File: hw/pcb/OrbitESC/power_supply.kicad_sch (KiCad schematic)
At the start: 0 parts

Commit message: Add power stage components
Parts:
- added C22, C24, C28: 100nF, Capacitor_SMD:C_0402_1005Metric, symbol Device:C
- added C23, C25, C26: 10uF, Capacitor_SMD:C_0805_2012Metric, symbol Device:C
- added C27, C29: 2.2uF, Capacitor_SMD:C_0805_2012Metric, symbol Device:C
- added D1, D3, D4: Blue LED, Diode_SMD:D_0603_1608Metric, symbol Device:LED
- added D2: 18v, Diode_SMD:D_SMA, symbol Device:D_Zener
- added FB1: FerriteBead_Small, Resistor_SMD:R_0603_1608Metric, symbol Device:FerriteBead_Small
- added L1: 4.7uH, Inductor_SMD:L_Bourns-SRN6028, symbol Device:L
- added Q7: 2N7002, Package_TO_SOT_SMD:SOT-23, symbol Transistor_FET:2N7002
- added R37, R38, R41, R44: 10k, Resistor_SMD:R_0402_1005Metric, symbol Device:R_US
- added R39: 1k, Resistor_SMD:R_0402_1005Metric, symbol Device:R_US
- added R40: 51k, Resistor_SMD:R_0402_1005Metric, symbol Device:R_US
- added R42: 10, Resistor_SMD:R_0402_1005Metric, symbol Device:R_US
- added R43: 1.5k, Resistor_SMD:R_0402_1005Metric, symbol Device:R_US
- added R45: 200, Resistor_SMD:R_0402_1005Metric, symbol Device:R_US
- added R46: 49.9, Resistor_SMD:R_0402_1005Metric, symbol Device:R_US
- added U7: AP62200Z6-7, Package_TO_SOT_SMD:SOT-563, symbol Regulator_Switching:AP62250Z6
- added U8: AP2171W, Package_TO_SOT_SMD:SOT-23-5, symbol Power_Management:AP2171W
- added U9: AP2120, Package_TO_SOT_SMD:SOT-23, symbol Regulator_Linear:AP2127N-3.3
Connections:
- new net: R37.2, U7.5 (EN)
- new net: D4.2 (A), R46.2
- new net: D3.2 (A), R45.2
- new net: R40.2, R41.2, U7.6 (FB)
- new net: C24.1, L1.1, U7.2 (SW)
- new net: C24.2, U7.4 (BST)
- new net: FB1.2, R42.1
- new net: D1.2 (A), R43.2
- new net: Q7.1 (G), R38.2, R39.2
- new net: Q7.3 (D), R44.2, U8.4 (EN)
- new net +3.3V: C29.2, FB1.1, R46.1, U9.2 (VO)
- new net +3.3VADC: C27.2, C28.1, R42.2
- new net +5V: C25.1, C26.1, L1.2, R40.1, R45.1, U8.1 (OUT), U9.3 (VI)
- new net GNDD: C22.1, C23.2, C25.2, C26.2, C27.1, C28.2, C29.1, D1.1 (K), D2.2 (A), D3.1 (K), D4.1 (K), Q7.2 (S), R38.1, R41.1, U7.3 (GND), U8.2 (GND), U9.1 (GND)
- new net VBUS: R44.1, U8.5 (IN)
- new net VDC: C22.2, C23.1, D2.1 (K), R37.1, R39.1, R43.1, U7.1 (VIN)
- no-connect marks 0 -> 1
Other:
- note added: "Buck Converter"
- note added: "USB Power Select"

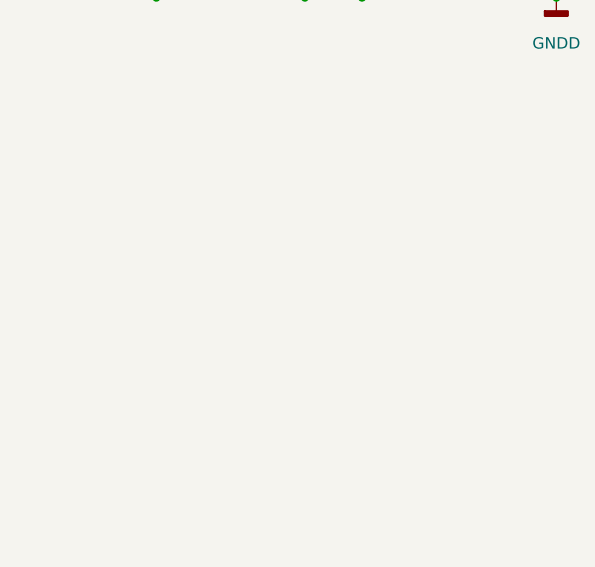
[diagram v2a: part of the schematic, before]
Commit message: Start routing power stage
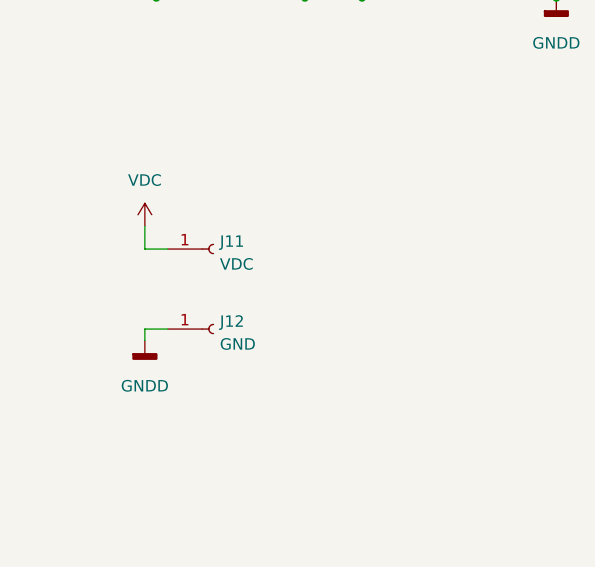
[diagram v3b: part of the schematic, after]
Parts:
- added J11: VDC, TestPoint:TestPoint_Pad_4.0x4.0mm, symbol Connector:Conn_01x01_Female
- added J12: GND, TestPoint:TestPoint_Pad_4.0x4.0mm, symbol Connector:Conn_01x01_Female
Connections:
- net GNDD: now also J12.1 (Pin_1)
- net VDC: now also J11.1 (Pin_1)
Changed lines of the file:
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@@
+    (stroke (width 0) (type default) (color 0 0 0 0))
+  )
+  (wire (pts (xy 54.61 95.25) (xy 54.61 97.79))
     (stroke (width 0) (type default) (color 0 0 0 0))
   )
@@
     (stroke (width 0) (type default) (color 0 0 0 0))
   )
+  (wire (pts (xy 54.61 106.68) (xy 57.15 106.68))
+    (stroke (width 0) (type default) (color 0 0 0 0))
+  )
   (wire (pts (xy 87.63 41.91) (xy 78.74 41.91))
     (stroke (width 0) (type default) (color 0 0 0 0))
@@
     (stroke (width 0) (type default) (color 0 0 0 0))
   )
+  (wire (pts (xy 54.61 107.95) (xy 54.61 106.68))
+    (stroke (width 0) (type default) (color 0 0 0 0))
+  )
   (wire (pts (xy 168.91 69.85) (xy 157.48 69.85))
     (stroke (width 0) (type default) (color 0 0 0 0))
@@
   )
   (wire (pts (xy 146.05 54.61) (xy 146.05 55.88))
+    (stroke (width 0) (type default) (color 0 0 0 0))
+  )
+  (wire (pts (xy 54.61 97.79) (xy 57.15 97.79))
     (stroke (width 0) (type default) (color 0 0 0 0))
   )
@@
     (pin "2")
   )
+  (symbol (lib_id "power:VDC") (at 54.61 95.25 0) (unit 1)
+    (in_bom yes) (on_board yes)
+    (property "Reference" "#PWR0139" (id 0) (at 54.61 97.79 0)
+      (effects (font (size 1.27 1.27)) hide)
+    )
+    (property "Value" "VDC" (id 1) (at 54.61 90.17 0))
+    (property "Footprint" "" (id 2) (at 54.61 95.25 0)
+      (effects (font (size 1.27 1.27)) hide)
+    )
+    (property "Datasheet" "" (id 3) (at 54.61 95.25 0)
+      (effects (font (size 1.27 1.27)) hide)
+    )
+    (pin "1")
+  )
   (symbol (lib_id "Regulator_Switching:AP62250Z6") (at 111.76 44.45 0) (unit 1)
     (in_bom yes) (on_board yes) (fields_autoplaced)
@@
     (pin "2")
   )
+  (symbol (lib_id "Connector:Conn_01x01_Female") (at 62.23 106.68 0) (unit 1)
+    (in_bom yes) (on_board yes) (fields_autoplaced)
+    (property "Reference" "J12" (id 0) (at 62.9412 105.8453 0)
+      (effects (font (size 1.27 1.27)) (justify left))
+    )
+    (property "Value" "GND" (id 1) (at 62.9412 108.3822 0)
+      (effects (font (size 1.27 1.27)) (justify left))
+    )
+    (property "Footprint" "TestPoint:TestPoint_Pad_4.0x4.0mm" (id 2) (at 62.23 106.68 0)
+      (effects (font (size 1.27 1.27)) hide)
+    )
+    (property "Datasheet" "~" (id 3) (at 62.23 106.68 0)
+      (effects (font (size 1.27 1.27)) hide)
+    )
+    (property "DigiKey" "N/A" (id 4) (at 62.23 106.68 0)
+      (effects (font (size 1.27 1.27)) hide)
+    )
+    (pin "1")
+  )
   (symbol (lib_id "Device:LED") (at 41.91 59.69 90) (unit 1)
     (in_bom yes) (on_board yes) (fields_autoplaced)
@@
     )
     (property "Datasheet" "" (id 3) (at 100.33 69.85 0)
+      (effects (font (size 1.27 1.27)) hide)
+    )
+    (pin "1")
+  )
+  (symbol (lib_id "Connector:Conn_01x01_Female") (at 62.23 97.79 0) (unit 1)
+    (in_bom yes) (on_board yes) (fields_autoplaced)
+    (property "Reference" "J11" (id 0) (at 62.9412 96.9553 0)
+      (effects (font (size 1.27 1.27)) (justify left))
+    )
+    (property "Value" "VDC" (id 1) (at 62.9412 99.4922 0)
+      (effects (font (size 1.27 1.27)) (justify left))
+    )
+    (property "Footprint" "TestPoint:TestPoint_Pad_4.0x4.0mm" (id 2) (at 62.23 97.79 0)
+      (effects (font (size 1.27 1.27)) hide)
+    )
+    (property "Datasheet" "~" (id 3) (at 62.23 97.79 0)
+      (effects (font (size 1.27 1.27)) hide)
+    )
+    (property "DigiKey" "N/A" (id 4) (at 62.23 97.79 0)
       (effects (font (size 1.27 1.27)) hide)
     )
@@
       (effects (font (size 1.27 1.27)) hide)
     )
+    (pin "1")
+  )
+  (symbol (lib_id "power:GNDD") (at 54.61 107.95 0) (unit 1)
+    (in_bom yes) (on_board yes) (fields_autoplaced)
+    (property "Reference" "#PWR0140" (id 0) (at 54.61 114.3 0)
+      (effects (font (size 1.27 1.27)) hide)
+    )
+    (property "Value" "GNDD" (id 1) (at 54.61 113.03 0))
+    (property "Footprint" "" (id 2) (at 54.61 107.95 0)
+      (effects (font (size 1.27 1.27)) hide)
+    )
+    (property "Datasheet" "" (id 3) (at 54.61 107.95 0)
+      (effects (font (size 1.27 1.27)) hide)
+    )

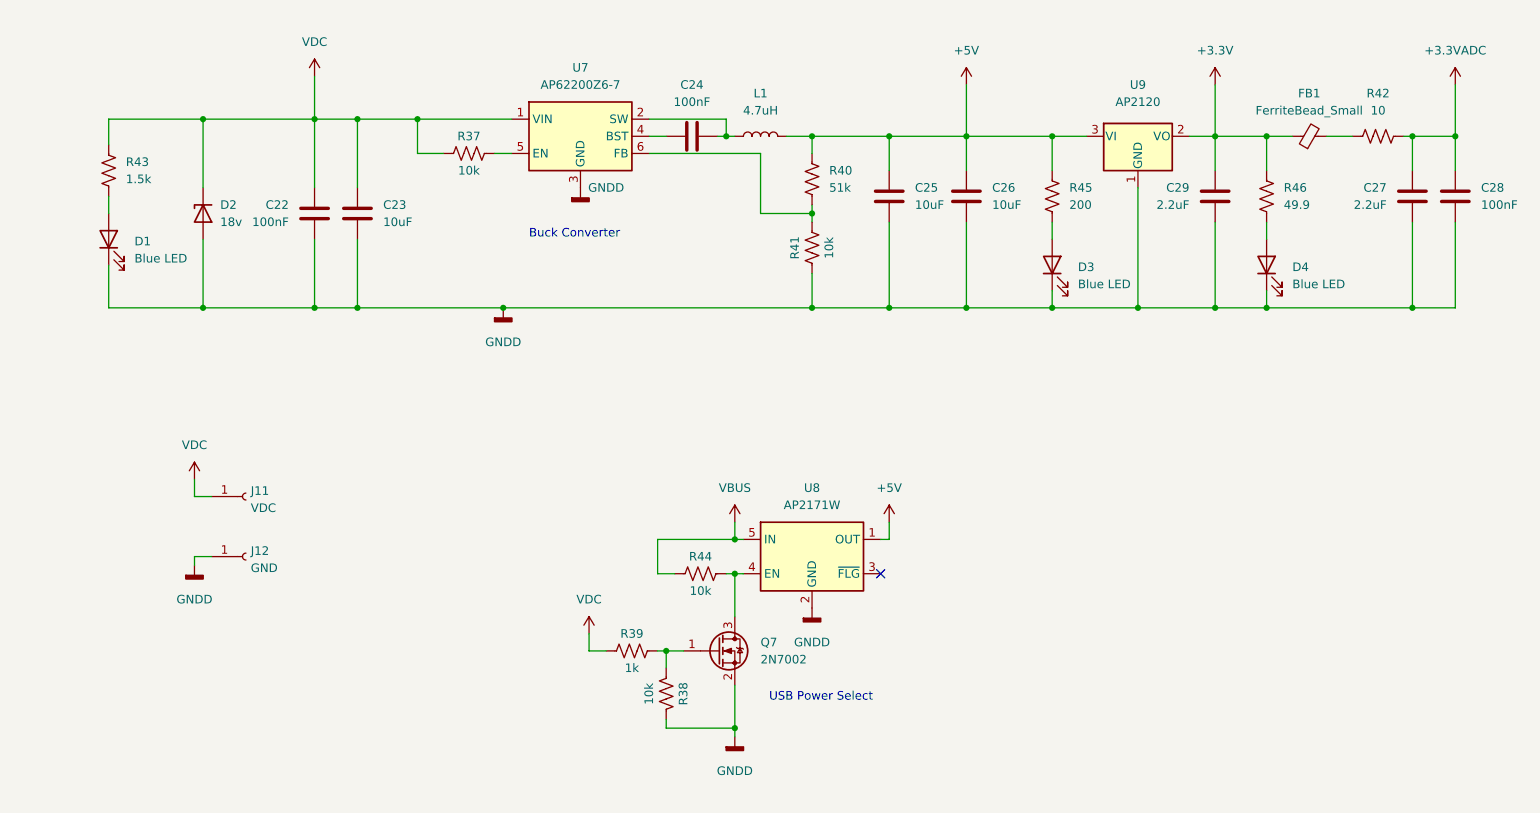
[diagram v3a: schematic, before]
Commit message: Save a few board changes found when assembing PCB v1.0
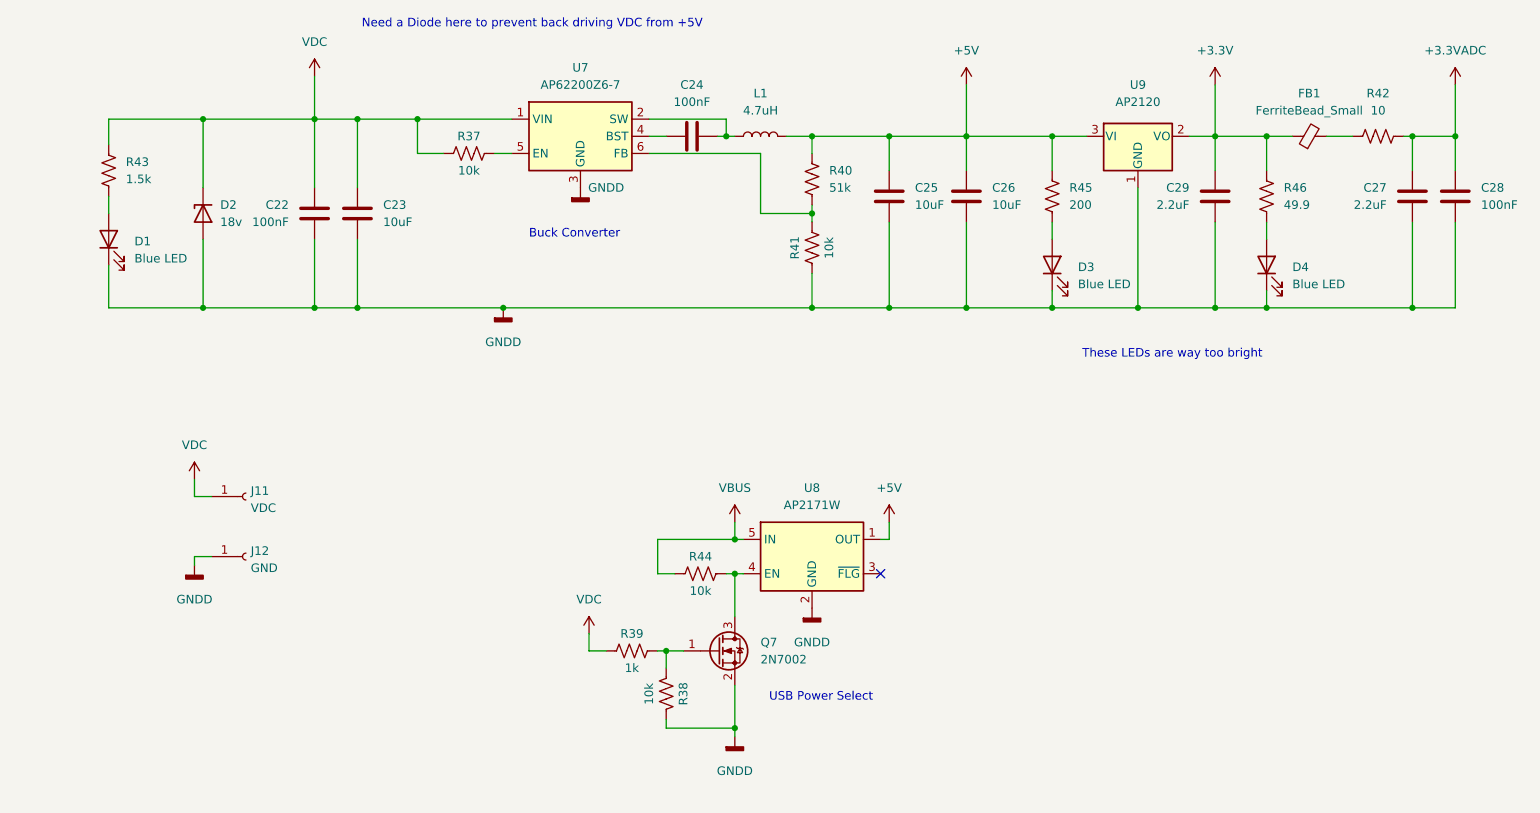
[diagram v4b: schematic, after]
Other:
- note added: "Need a Diode here to prevent back driving VDC from +5V"
- note added: "These LEDs are way too bright"
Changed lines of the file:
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@@
+    (effects (font (size 1.27 1.27)) (justify left bottom))
+  )
+  (text "These LEDs are way too bright" (at 186.055 77.47 0)
+    (effects (font (size 1.27 1.27)) (justify left bottom))
+  )
+  (text "Need a Diode here to prevent back driving VDC from +5V\n"
+    (at 79.375 28.575 0)
     (effects (font (size 1.27 1.27)) (justify left bottom))
   )

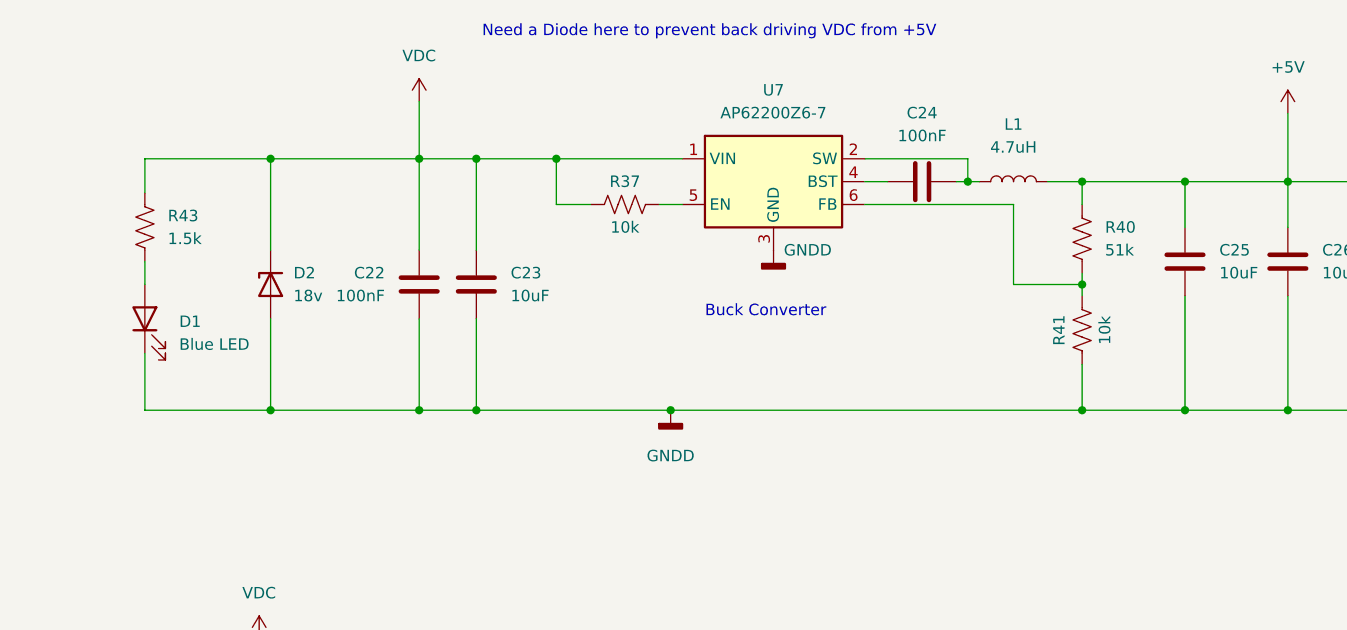
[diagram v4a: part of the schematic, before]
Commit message: Update a few issues with the analog and power stage
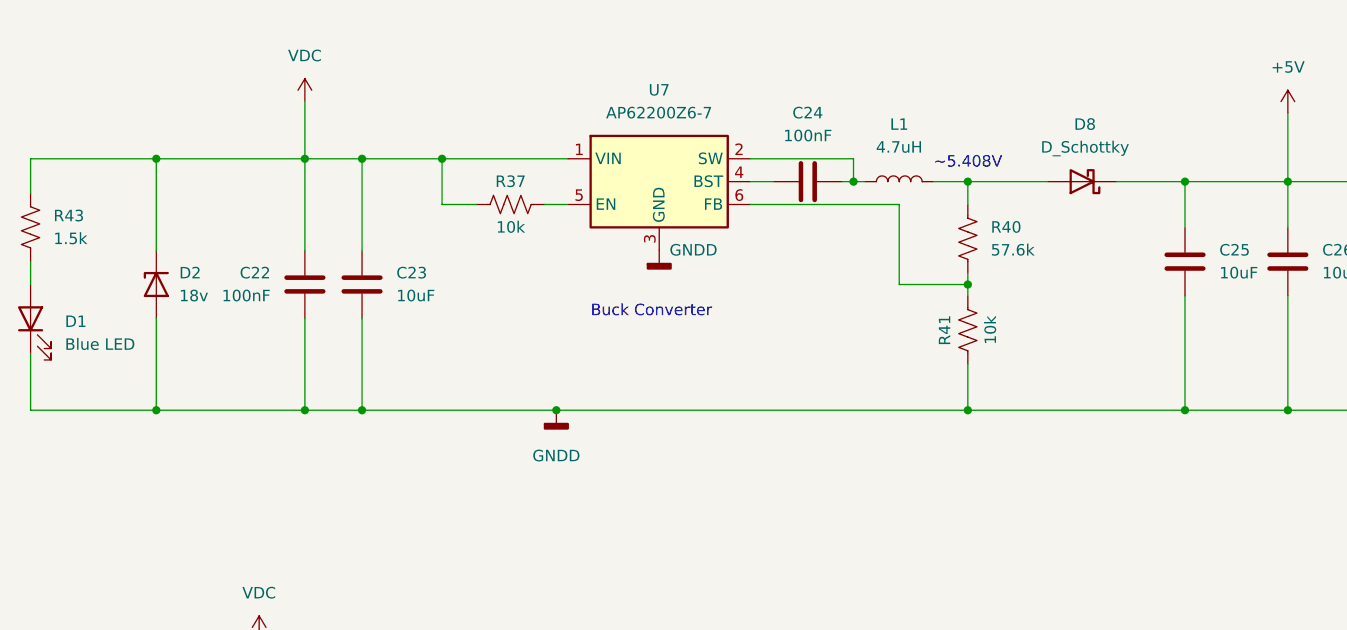
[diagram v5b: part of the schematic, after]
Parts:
- added D8: D_Schottky, symbol Device:D_Schottky
- R40: value 51k -> 57.6k; DigiKey (none) -> RMCF0402FT57K6CT-ND; JLCPCB C25794 -> N/A
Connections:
- net +5V: now also D8.1 (K); no longer L1.2, R40.1
- new net: D8.2 (A), L1.2, R40.1
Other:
- note added: "~5.408V"
- note removed: "Need a Diode here to prevent back driving VDC from +5V"
- moved on the sheet: C22, C23, C24, D1, D2, L1, R37, R40, R41, R43, U7

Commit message: Sync lunch schematic update
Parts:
- added C33: 2.2uF, Capacitor_SMD:C_0805_2012Metric, symbol Device:C
- added C34, C36: 100nF, Capacitor_SMD:C_0402_1005Metric, symbol Device:C
- added C37, C38, C40: 10uF, Capacitor_SMD:C_0805_2012Metric, symbol Device:C
- D8: value D_Schottky -> B5819W; footprint (none) -> Diode_SMD:D_SOD-123; JLCPCB (none) -> C8598
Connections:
- net +3.3V: now also C36.1
- net +5V: now also C33.2; no longer C25.1, C26.1
- net GNDD: now also C33.1, C34.2, C36.2, C37.2, C38.2, C40.2
- net at D8.2 (A), L1.2, R40.1: now also C25.1, C26.1, C34.1, C37.1, C38.1, C40.1
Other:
- moved on the sheet: C25, C26, C27, C28, C29, D3, D4, D8, FB1, Q7, R38, R39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

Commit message: Sync PCB updates
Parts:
- removed C37, C38, C40: 10uF, Capacitor_SMD:C_0805_2012Metric, symbol Device:C
- removed D3, D4: Blue LED, Diode_SMD:D_0603_1608Metric, symbol Device:LED
- removed R45: 200, Resistor_SMD:R_0402_1005Metric, symbol Device:R_US
- removed R46: 49.9, Resistor_SMD:R_0402_1005Metric, symbol Device:R_US
- C25, C26: value 10uF -> 47uF; JLCPCB C440198 -> C16780
- R40: value 57.6k -> 56k; JLCPCB N/A -> C25796
- R43: value 1.5k -> 10k; JLCPCB C25867 -> C25744
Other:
- note added: "~5.28V"
- note removed: "These LEDs are way too bright"
- note removed: "~5.408V"
- moved on the sheet: C22, C23, C24, C25, C26, C27, C28, C33, C34, D1, D2, D8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
